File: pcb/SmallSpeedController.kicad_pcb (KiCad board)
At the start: 4 copper layers, 30.7 x 51.7 mm, 38 parts, among them J1 Conn_01x02_Socket, J10 Conn_01x03_Socket, J11 Conn_01x03_Socket, J2 Conn_01x02_Socket, J4 Conn_01x02_Socket, J5 Conn_01x04_Socket, J6 Conn_01x04_Socket, J9 Conn_01x03_Socket, SW2 TS-1088-AR02016, U2 AMS1117-3.3, U3 DRV8837DSGR, U4 DRV8837DSGR, U5 CH32V003FxUx

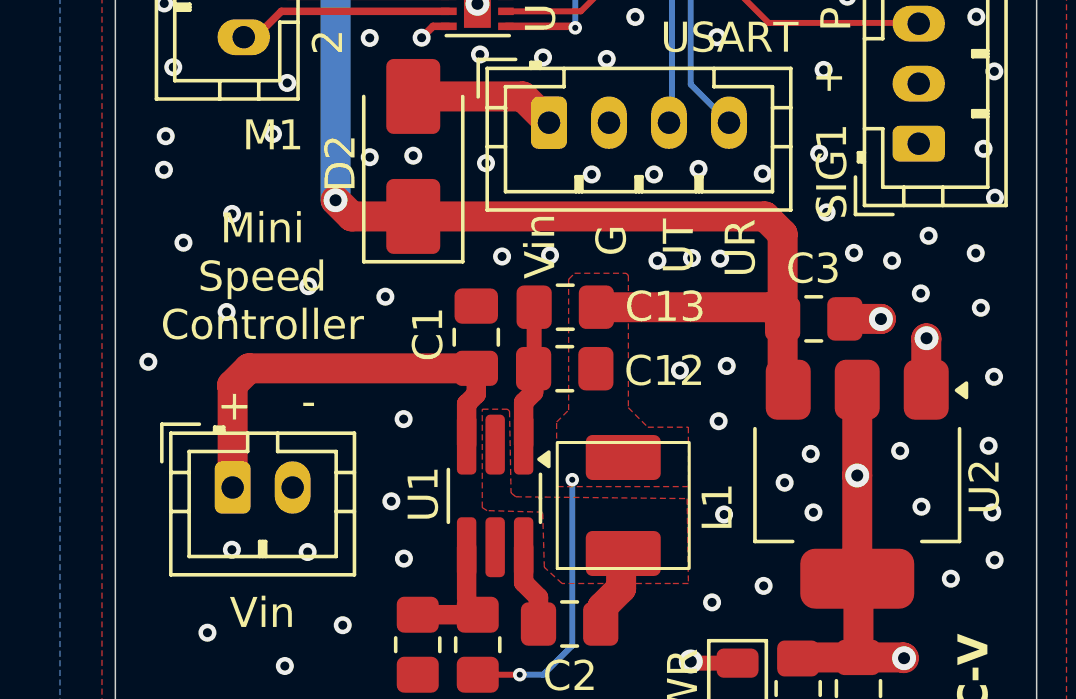
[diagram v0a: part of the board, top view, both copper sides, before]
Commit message: pcb: move silk prints around
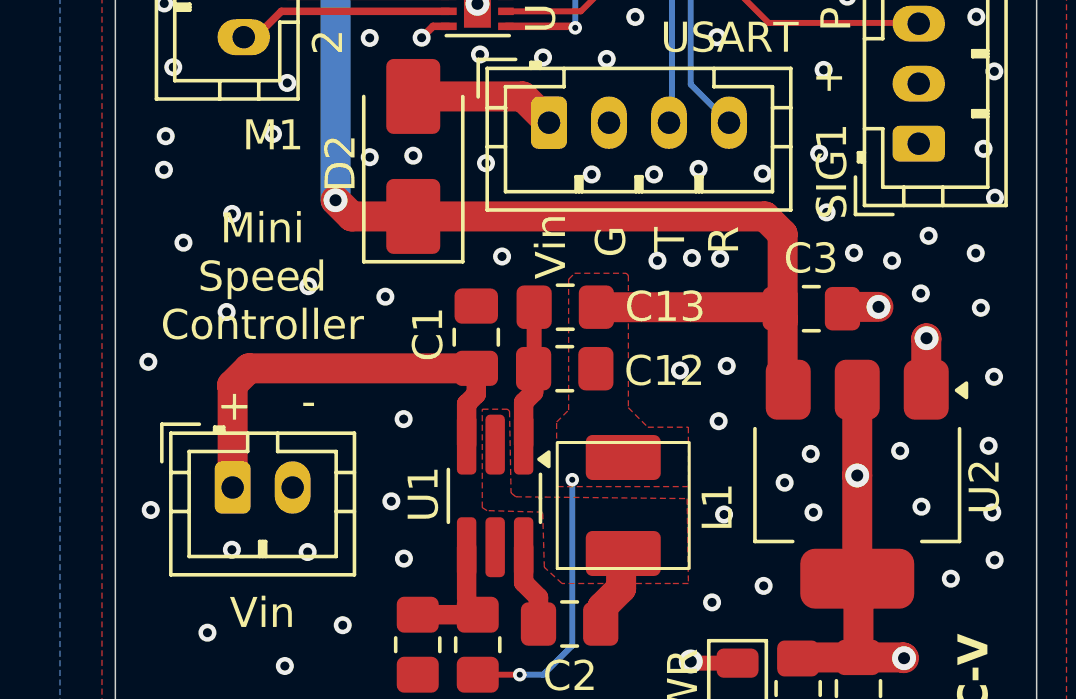
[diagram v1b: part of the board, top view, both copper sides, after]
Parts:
- moved C3 0.35 mm to (42.7, 102.8)
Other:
- board text added: "R"
- board text added: "T"
- board text removed: "UR"
- board text removed: "UT"
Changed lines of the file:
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@@
 	(footprint "Capacitor_SMD:C_0805_2012Metric_Pad1.18x1.45mm_HandSolder"
 		(layer "F.Cu")
-		(at 42.8 103.19)
+		(at 42.72 102.85)
 		(descr "Capacitor SMD 0805 (2012 Metric), square (rectangular) end terminal, IPC-7351 nominal with elongated pad for handsoldering. (Body size source: IPC-SM-782 page 76, https://www.pcb-3d.com/wordpress/wp-content/uploads/ipc-sm-782a_amendment_1_and_2.pdf, https://docs.google.com/spreadsheets/d/1BsfQQcO9C6DZCsRaXUlFlo91Tg2WpOkGARC1WS5S8t0/edit?usp=sharing), generated with kicad-footprint-generator")
 		(tags "capacitor handsolder")
@@
 	)
 	(gr_text "G"
-		(at 36.65 101.1 90)
+		(at 36.63 101.14 90)
 		(layer "F.SilkS")
 		(effects
@@
 		)
 	)
-	(gr_text "UR"
-		(at 40.95 101.81 90)
+	(gr_text "R"
+		(at 40.4 101.04 90)
 		(layer "F.SilkS")
 		(effects
@@
 		)
 	)
-	(gr_text "UT"
-		(at 38.89 101.69 90)
+	(gr_text "T"
+		(at 38.6 100.96 90)
 		(layer "F.SilkS")
 		(effects
@@
 	)
 	(gr_text "Vin"
-		(at 34.27 101.86 90)
+		(at 34.63 101.87 90)
 		(layer "F.SilkS")
 		(effects
@@
 	)
 	(segment
-		(start 43.8375 103.19)
-		(end 45.035 103.19)
+		(start 43.76125 102.79)
+		(end 44.95875 102.79)
 		(width 1)
 		(layer "F.Cu")
@@
 	)
 	(segment
-		(start 45.035 103.19)
-		(end 45.04 103.195)
-		(width 1)
-		(layer "F.Cu")
-		(net 2)
-	)
-	(segment
 		(start 39.15 84.25)
 		(end 38.1 84.25)
@@
 	)
 	(via
-		(at 45.04 103.195)
+		(at 44.95875 102.79)
 		(size 0.8)
 		(drill 0.4)
@@
 	)
 	(via
-		(at 34.01 101.07)
+		(at 20.7 109.56)
 		(size 0.6)
 		(drill 0.3)
